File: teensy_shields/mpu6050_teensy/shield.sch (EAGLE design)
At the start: 2 parts

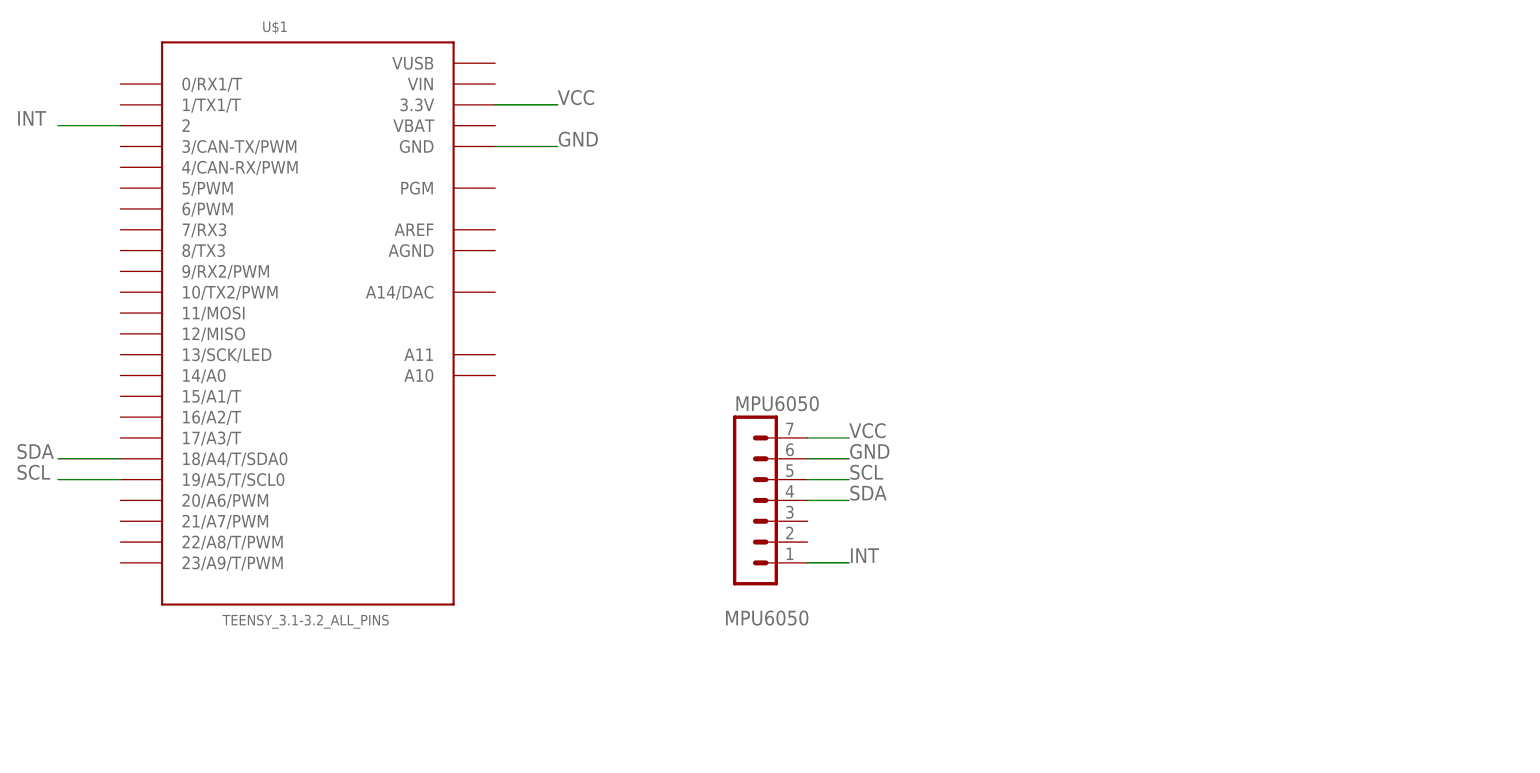
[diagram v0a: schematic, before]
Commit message: Cleaned up board
Added a pulldown resistor to the i2c channel select pin and cleaned up the the board.
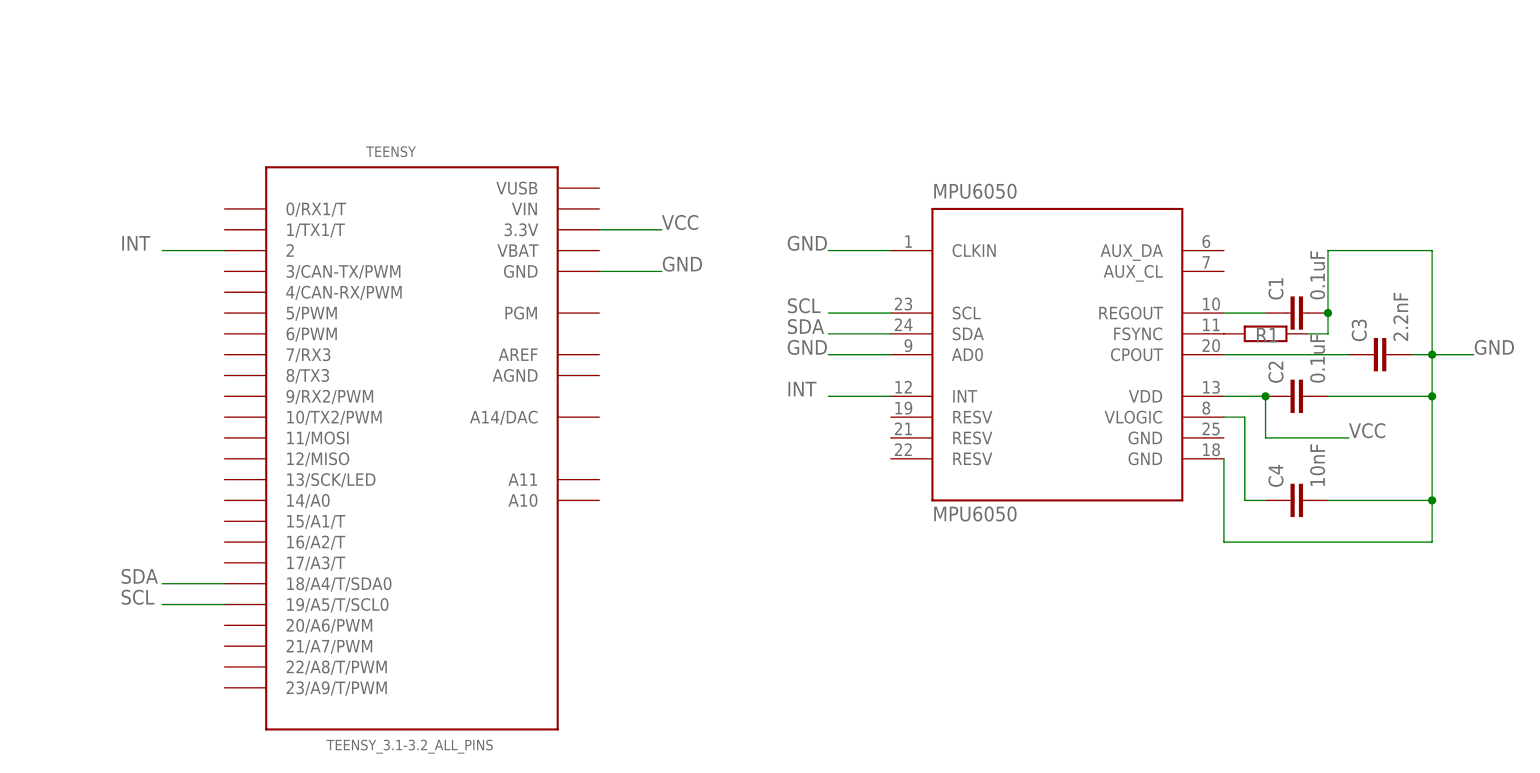
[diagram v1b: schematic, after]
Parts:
- removed U$1: TEENSY_3.1-3.2_ALL_PINS, Teensy:TEENSY_3.1-3.2_ALL_PINS
- added C1, C2: 0.1uF, SparkFun-Capacitors:0.1UF-0603-25V-(+80/-20%)
- added C3: 2.2nF, SparkFun-Capacitors:2.2NF/2200PF-0603-50V-10%
- added C4: 10nF, SparkFun-Capacitors:10NF-0603-50V-10%
- added R1: (no value), eagle-ltspice:RR0603
- added TEENSY: TEENSY_3.1-3.2_ALL_PINS, Teensy:TEENSY_3.1-3.2_ALL_PINS
- MPU6050: value (none) -> MPU6050; device con-lstb:MA07-1 -> invensense:MPU6050
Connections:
- new net N$1: C3.1, MPU6050G$1.CPOUT
- new net N$2: C1.1, MPU6050G$1.REGOUT
- new net N$3: C4.1, MPU6050G$1.VLOGIC
- new net N$4: MPU6050G$1.FSYNC, R1.1
- net GND: now also C1.2, C2.2, C3.2, C4.2, MPU6050G$1.AD0, MPU6050G$1.CLKIN, MPU6050G$1.GND, R1.2, TEENSY.GND; no longer MPU6050.6, U$1.GND
- net INT: now also MPU6050G$1.INT, TEENSY.2; no longer MPU6050.1, U$1.2
- net SCL: now also MPU6050G$1.SCL, TEENSY.19/A5/T/SCL0; no longer MPU6050.5, U$1.19/A5/T/SCL0
- net SDA: now also MPU6050G$1.SDA, TEENSY.18/A4/T/SDA0; no longer MPU6050.4, U$1.18/A4/T/SDA0
- net VCC: now also C2.1, MPU6050G$1.VDD, TEENSY.3.3V; no longer MPU6050.7, U$1.3.3V
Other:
- note removed: "MPU6050"

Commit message: Switched files
Corrected file directories
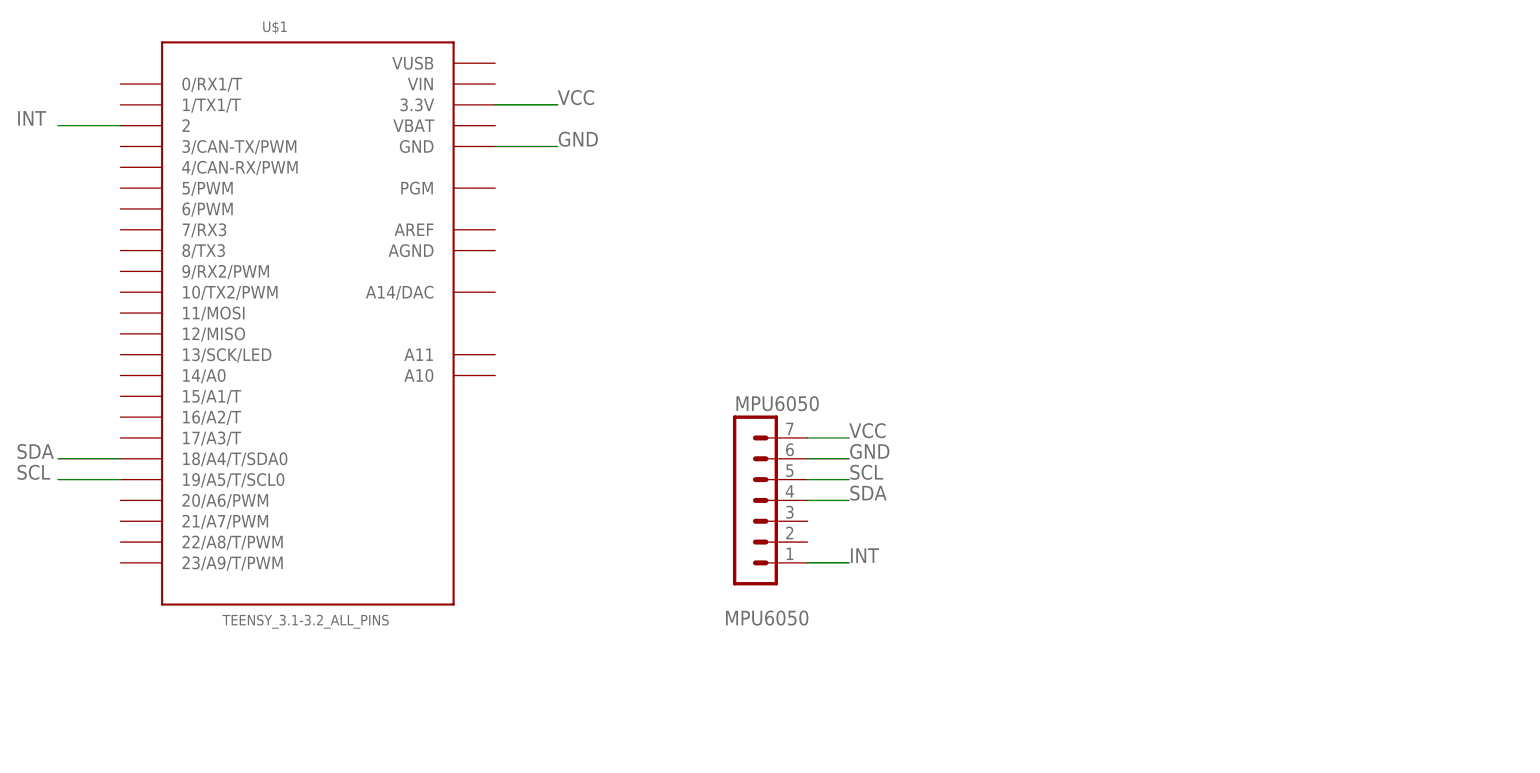
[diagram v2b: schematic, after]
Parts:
- removed C1, C2: 0.1uF, SparkFun-Capacitors:0.1UF-0603-25V-(+80/-20%)
- removed C3: 2.2nF, SparkFun-Capacitors:2.2NF/2200PF-0603-50V-10%
- removed C4: 10nF, SparkFun-Capacitors:10NF-0603-50V-10%
- removed R1: (no value), eagle-ltspice:RR0603
- removed TEENSY: TEENSY_3.1-3.2_ALL_PINS, Teensy:TEENSY_3.1-3.2_ALL_PINS
- added U$1: TEENSY_3.1-3.2_ALL_PINS, Teensy:TEENSY_3.1-3.2_ALL_PINS
- MPU6050: value MPU6050 -> (none); device invensense:MPU6050 -> con-lstb:MA07-1
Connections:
- removed net N$1: C3.1, MPU6050G$1.CPOUT
- removed net N$2: C1.1, MPU6050G$1.REGOUT
- removed net N$3: C4.1, MPU6050G$1.VLOGIC
- removed net N$4: MPU6050G$1.FSYNC, R1.1
- net GND: now also MPU6050.6, U$1.GND; no longer C1.2, C2.2, C3.2, C4.2, MPU6050G$1.AD0, MPU6050G$1.CLKIN, MPU6050G$1.GND, R1.2, TEENSY.GND
- net INT: now also MPU6050.1, U$1.2; no longer MPU6050G$1.INT, TEENSY.2
- net SCL: now also MPU6050.5, U$1.19/A5/T/SCL0; no longer MPU6050G$1.SCL, TEENSY.19/A5/T/SCL0
- net SDA: now also MPU6050.4, U$1.18/A4/T/SDA0; no longer MPU6050G$1.SDA, TEENSY.18/A4/T/SDA0
- net VCC: now also MPU6050.7, U$1.3.3V; no longer C2.1, MPU6050G$1.VDD, TEENSY.3.3V
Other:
- note added: "MPU6050"
